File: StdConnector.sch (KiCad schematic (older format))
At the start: 29 parts, among them P1 CONN_01X02, P2 FDSP_Header, P3 StdConn_ClkOut, P4 StsConn_ClkOut, P5 StdConn_ClkVar, P6 StdConn_ClkIn, U1 74HC14, U2 LM2574, Y1 12.288MHz

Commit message: Changed Connector position to fit old board. HF Lines optimized.
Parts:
- added D?: D_Schottky, Diodes_ThroughHole:Diode_DO-35_SOD27_Horizontal_RM10, symbol D_Schottky
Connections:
- net +12V: now also D?.1 (K); no longer P1.2 (P2)
- new net: D?.2 (A), P1.2 (P2)
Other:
- moved on the sheet: P1
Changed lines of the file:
@@
 	4450 3600 3750 3600
 Wire Wire Line
-	2300 3600 3250 3600
+	2300 3600 2400 3600
+Wire Wire Line
+	2400 3600 3250 3600
 $Comp
 L GND #PWR03
@@
 	4450 4600 3750 4600
 Wire Wire Line
-	2300 4600 3250 4600
+	2300 4600 2400 4600
+Wire Wire Line
+	2400 4600 3250 4600
 Wire Wire Line
 	4650 4500 3750 4500
@@
 $EndComp
 Wire Wire Line
-	3000 1200 3500 1200
-Wire Wire Line
-	2000 1200 2000 2200
+	3000 1200 3100 1200
+Wire Wire Line
+	3100 1200 3400 1200
+Wire Wire Line
+	3400 1200 3500 1200
+Wire Wire Line
+	2000 1200 2000 1600
+Wire Wire Line
+	2000 1600 2000 2100
+Wire Wire Line
+	2000 2100 2000 2200
 Wire Wire Line
 	2000 1200 2100 1200
@@
 	2700 1600 3100 1600
 Wire Wire Line
-	3100 2000 3100 2200
-Wire Wire Line
-	3100 1200 3100 1700
+	3100 2000 3100 2100
+Wire Wire Line
+	3100 2100 3100 2200
+Wire Wire Line
+	3100 1200 3100 1600
+Wire Wire Line
+	3100 1600 3100 1700
 Connection ~ 3100 1200
 Connection ~ 3100 1600
@@
 	3400 2800 3500 2800
 Wire Wire Line
-	3400 1200 3400 2800
+	3400 1200 3400 1600
+Wire Wire Line
+	3400 1600 3400 2000
+Wire Wire Line
+	3400 2000 3400 2400
+Wire Wire Line
+	3400 2400 3400 2800
 Connection ~ 3400 1200
 Connection ~ 3400 1600
@@
 L CONN_01X02 P1
 U 1 1 57268478
-P 1600 5850
-F 0 "P1" H 1600 6000 50  0000 C CNN
-F 1 "CONN_01X02" V 1700 5850 50  0000 C CNN
-F 2 "Connect:bornier2" H 1600 5850 60  0001 C CNN
-F 3 "" H 1600 5850 60  0000 C CNN
-	1    1600 5850
+P 1300 5850
+F 0 "P1" H 1300 6000 50  0000 C CNN
+F 1 "CONN_01X02" V 1400 5850 50  0000 C CNN
+F 2 "Connect:bornier2" H 1300 5850 60  0001 C CNN
+F 3 "" H 1300 5850 60  0000 C CNN
+	1    1300 5850
 	-1   0    0    1
 $EndComp
@@
 	4900 5800 4900 5900
 Wire Wire Line
-	4500 5800 5200 5800
+	4500 5800 4600 5800
+Wire Wire Line
+	4600 5800 4900 5800
+Wire Wire Line
+	4900 5800 5200 5800
 Wire Wire Line
 	4600 5800 4600 5900
 Connection ~ 4600 5800
 Wire Wire Line
-	3700 5800 3900 5800
-Wire Wire Line
-	1800 5800 2600 5800
+	3700 5800 3800 5800
+Wire Wire Line
+	3800 5800 3900 5800
+Wire Wire Line
+	2000 5800 2200 5800
+Wire Wire Line
+	2200 5800 2500 5800
+Wire Wire Line
+	2500 5800 2600 5800
 Wire Wire Line
 	2500 5800 2500 5900
 Wire Wire Line
-	2200 5700 2200 5900
+	2200 5700 2200 5800
+Wire Wire Line
+	2200 5800 2200 5900
 Connection ~ 2500 5800
 Connection ~ 2200 5800
@@
 $EndComp
 Wire Wire Line
-	1800 5900 1900 5900
-Wire Wire Line
-	1900 5900 1900 6300
-Wire Wire Line
-	1900 6300 2500 6300
+	1500 5900 1600 5900
+Wire Wire Line
+	1600 5900 1600 6300
+Wire Wire Line
+	1600 6300 2200 6300
+Wire Wire Line
+	2200 6300 2500 6300
 Wire Wire Line
 	2500 6300 2500 6200
 Wire Wire Line
-	2200 6200 2200 6400
+	2200 6200 2200 6300
+Wire Wire Line
+	2200 6300 2200 6400
 Connection ~ 2200 6300
 $Comp
@@
 	3350 6600 3350 6500
 Wire Wire Line
-	2950 6600 3350 6600
+	2950 6600 3150 6600
+Wire Wire Line
+	3150 6600 3350 6600
 Wire Wire Line
 	2950 6600 2950 6500
 Wire Wire Line
-	3150 6500 3150 6700
+	3150 6500 3150 6600
+Wire Wire Line
+	3150 6600 3150 6700
 Connection ~ 3150 6600
 $Comp
@@
 	3800 6200 3800 6300
 Wire Wire Line
-	3800 6300 4900 6300
+	3800 6300 4600 6300
+Wire Wire Line
+	4600 6300 4900 6300
 Wire Wire Line
 	4900 6300 4900 6200
 Wire Wire Line
-	4600 6200 4600 6400
+	4600 6200 4600 6300
+Wire Wire Line
+	4600 6300 4600 6400
 Connection ~ 4600 6300
 Wire Wire Line
-	5200 5700 5200 5900
+	5200 5700 5200 5800
+Wire Wire Line
+	5200 5800 5200 5900
 Connection ~ 4900 5800
 Wire Wire Line
-	5200 6200 5200 6400
+	5200 6200 5200 6300
+Wire Wire Line
+	5200 6300 5200 6400
 Wire Wire Line
 	5200 6800 5200 6700
@@
 $EndComp
 Wire Wire Line
-	9800 1500 9800 2600
+	9800 1500 9800 1800
+Wire Wire Line
+	9800 1800 9800 1900
+Wire Wire Line
+	9800 1900 9800 2000
+Wire Wire Line
+	9800 2000 9800 2100
+Wire Wire Line
+	9800 2100 9800 2200
+Wire Wire Line
+	9800 2200 9800 2300
+Wire Wire Line
+	9800 2300 9800 2400
+Wire Wire Line
+	9800 2400 9800 2500
+Wire Wire Line
+	9800 2500 9800 2600
 Wire Wire Line
 	9800 1800 9700 1800
@@
 Connection ~ 9800 1800
 Wire Wire Line
-	9100 1400 9100 1800
+	9100 1400 9100 1500
+Wire Wire Line
+	9100 1500 9100 1800
 Wire Wire Line
 	9100 1800 9200 1800
@@
 $EndComp
 Wire Wire Line
-	7200 3700 7200 4800
+	7200 3700 7200 4000
+Wire Wire Line
+	7200 4000 7200 4100
+Wire Wire Line
+	7200 4100 7200 4200
+Wire Wire Line
+	7200 4200 7200 4300
+Wire Wire Line
+	7200 4300 7200 4400
+Wire Wire Line
+	7200 4400 7200 4500
+Wire Wire Line
+	7200 4500 7200 4600
+Wire Wire Line
+	7200 4600 7200 4700
+Wire Wire Line
+	7200 4700 7200 4800
 Wire Wire Line
 	7200 4000 7100 4000
@@
 Connection ~ 7200 4000
 Wire Wire Line
-	6500 3600 6500 4000
+	6500 3600 6500 3700
+Wire Wire Line
+	6500 3700 6500 4000
 Wire Wire Line
 	6500 4000 6600 4000
@@
 $EndComp
 Wire Wire Line
-	10600 3700 10600 4800
+	10600 3700 10600 4000
+Wire Wire Line
+	10600 4000 10600 4100
+Wire Wire Line
+	10600 4100 10600 4200
+Wire Wire Line
+	10600 4200 10600 4300
+Wire Wire Line
+	10600 4300 10600 4400
+Wire Wire Line
+	10600 4400 10600 4500
+Wire Wire Line
+	10600 4500 10600 4600
+Wire Wire Line
+	10600 4600 10600 4700
+Wire Wire Line
+	10600 4700 10600 4800
 Wire Wire Line
 	10600 4000 10500 4000
@@
 Connection ~ 10600 4000
 Wire Wire Line
-	9900 3600 9900 4000
+	9900 3600 9900 3700
+Wire Wire Line
+	9900 3700 9900 4000
 Wire Wire Line
 	9900 4000 10000 4000
@@
 $EndComp
 Wire Wire Line
-	8900 3700 8900 4800
+	8900 3700 8900 4000
+Wire Wire Line
+	8900 4000 8900 4100
+Wire Wire Line
+	8900 4100 8900 4200
+Wire Wire Line
+	8900 4200 8900 4300
+Wire Wire Line
+	8900 4300 8900 4400
+Wire Wire Line
+	8900 4400 8900 4500
+Wire Wire Line
+	8900 4500 8900 4600
+Wire Wire Line
+	8900 4600 8900 4700
+Wire Wire Line
+	8900 4700 8900 4800
 Wire Wire Line
 	8900 4000 8800 4000
@@
 Connection ~ 8900 4000
 Wire Wire Line
-	8200 3600 8200 4000
+	8200 3600 8200 3700
+Wire Wire Line
+	8200 3700 8200 4000
 Wire Wire Line
 	8200 4000 8300 4000
@@
 	5300 1700 5300 1800
 Wire Wire Line
-	5300 1800 5500 1800
+	5300 1800 5400 1800
+Wire Wire Line
+	5400 1800 5500 1800
 Wire Wire Line
 	5500 1800 5500 1700
@@
 Wire Wire Line
 	5400 2200 5400 2300
+$Comp
+L D_Schottky D?
+U 1 1 57348F14
+P 1850 5800
+F 0 "D?" H 1850 5900 50  0000 C CNN
+F 1 "D_Schottky" H 1850 5700 50  0000 C CNN
+F 2 "Diodes_ThroughHole:Diode_DO-35_SOD27_Horizontal_RM10" H 1850 5800 60  0001 C CNN
+F 3 "" H 1850 5800 60  0000 C CNN
+	1    1850 5800
+	-1   0    0    1
+$EndComp
+Wire Wire Line
+	1700 5800 1500 5800
 $EndSCHEMATC

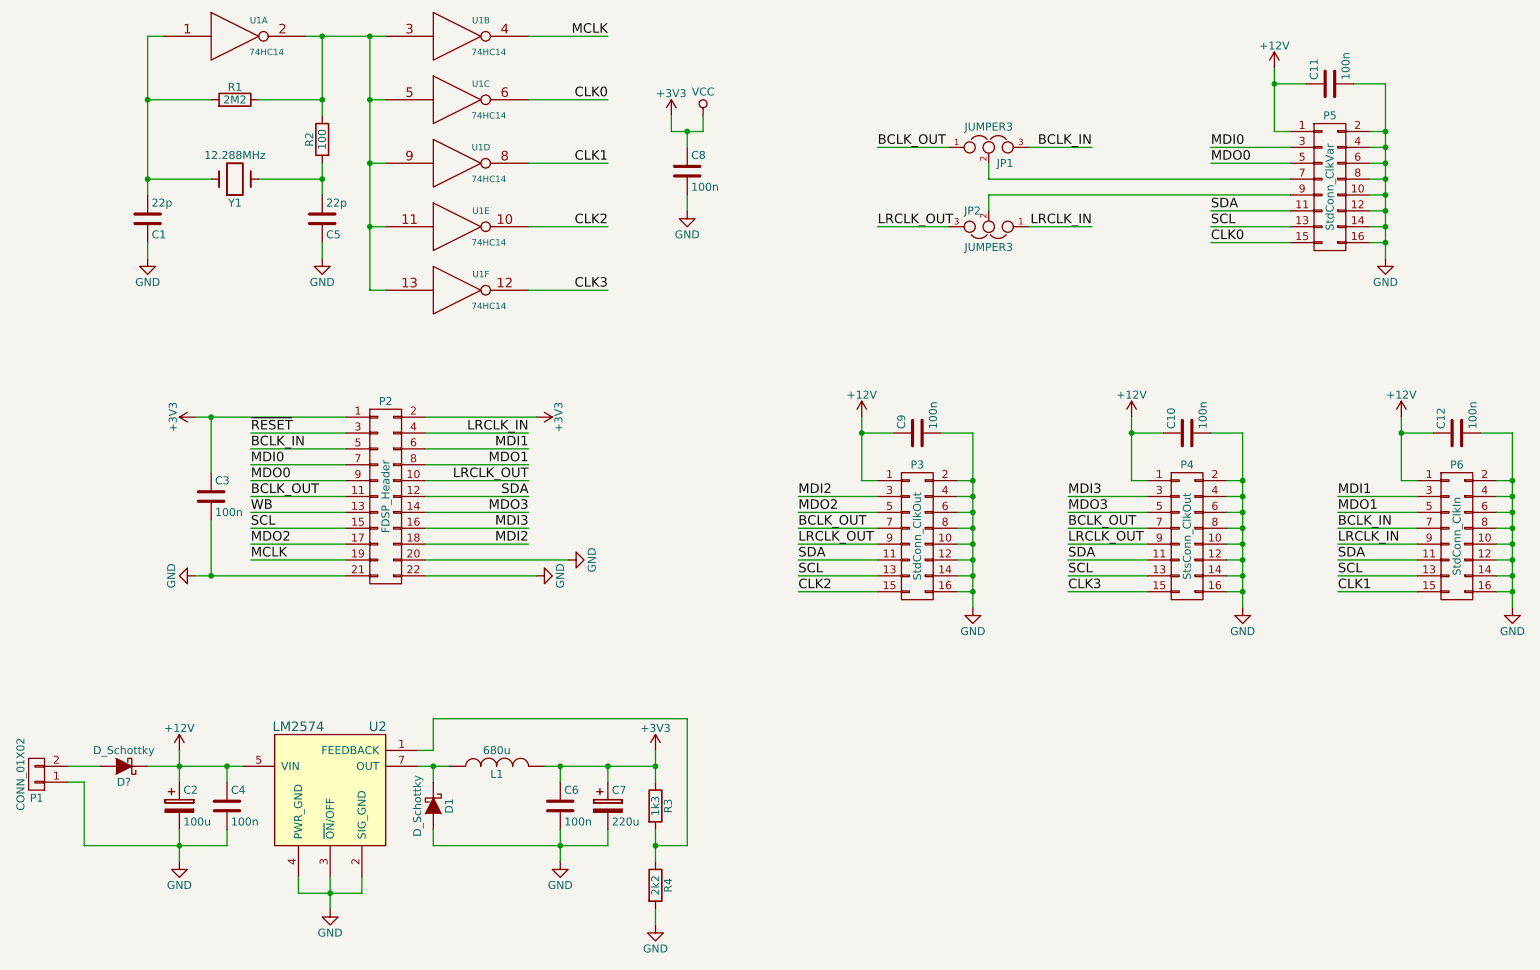
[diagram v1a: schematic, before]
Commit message: Corrected resistor value error in stepdown feedback.
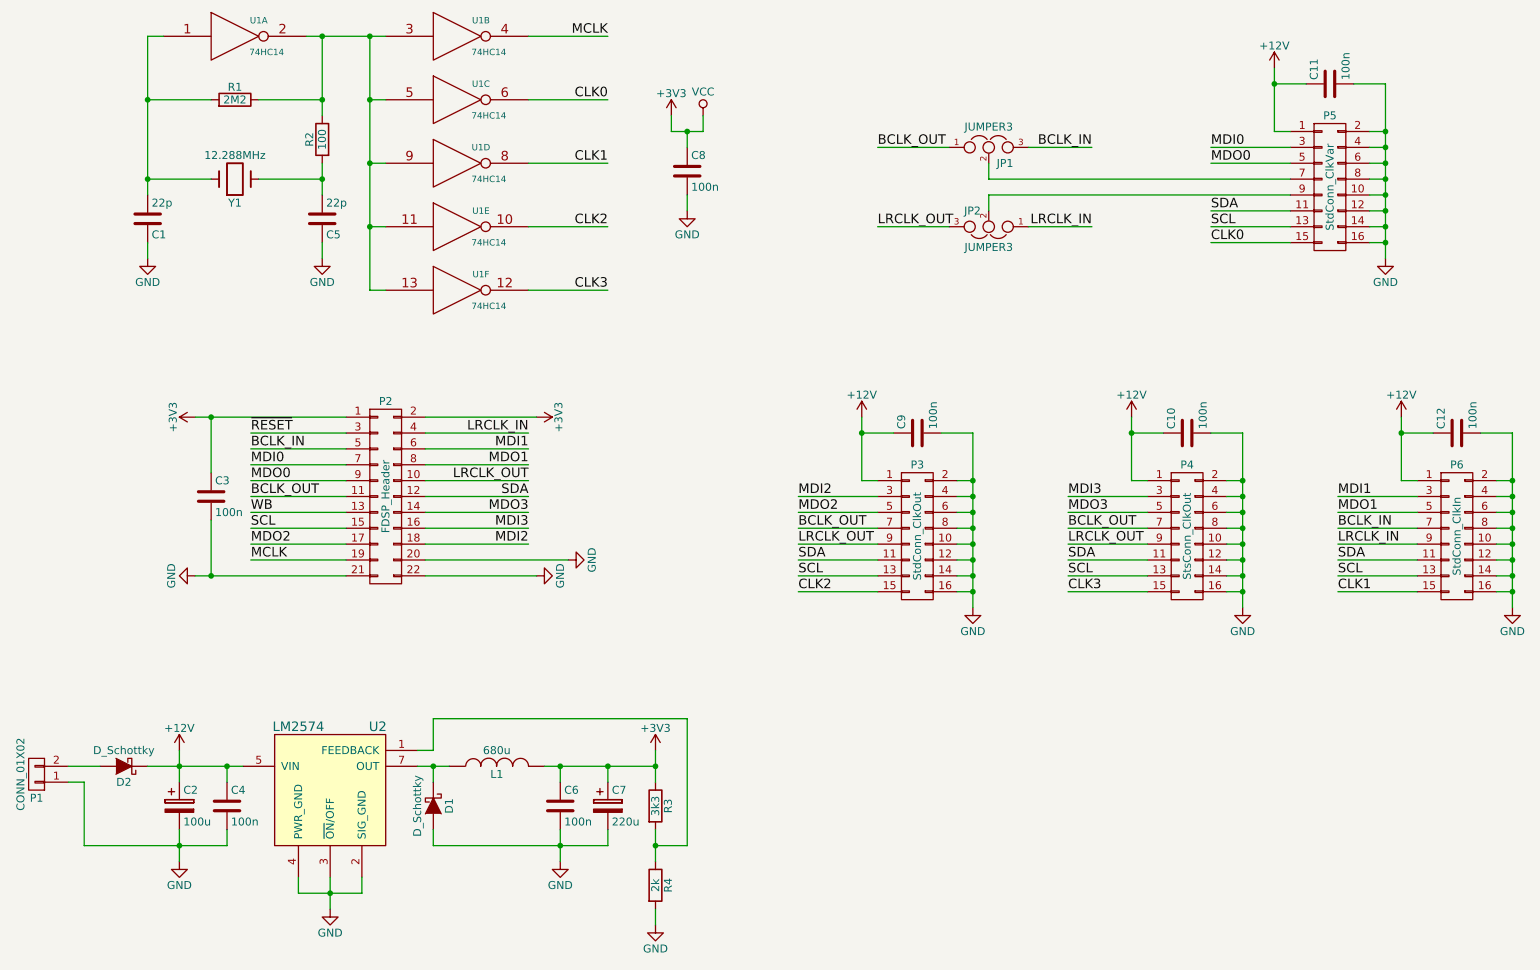
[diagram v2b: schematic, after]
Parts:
- R3: value 1k3 -> 3k3
- R4: value 2k2 -> 2k
- gave numbers to parts that had none: 1
